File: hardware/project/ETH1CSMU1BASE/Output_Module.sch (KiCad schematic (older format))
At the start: 64 parts

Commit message: Power supply design
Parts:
- removed HS?: Heatsink, symbol Mechanical:Heatsink
- added HS901: Heatsink_Pad, symbol Mechanical:Heatsink_Pad
- C910, C911: renamed from C?; value 10n -> 10n/400V
- Q915, Q916: renamed from Q?; value Q_PMOS_GDS -> IRF9630SPBF
- R925, R926: renamed from R?; value 26R1/10W -> 26R1/5W
- gave numbers to parts that had none: 57
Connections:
- net labels added: GNDF, GNDO
- net labels removed: GNDHV
- wire segments 209 -> 211

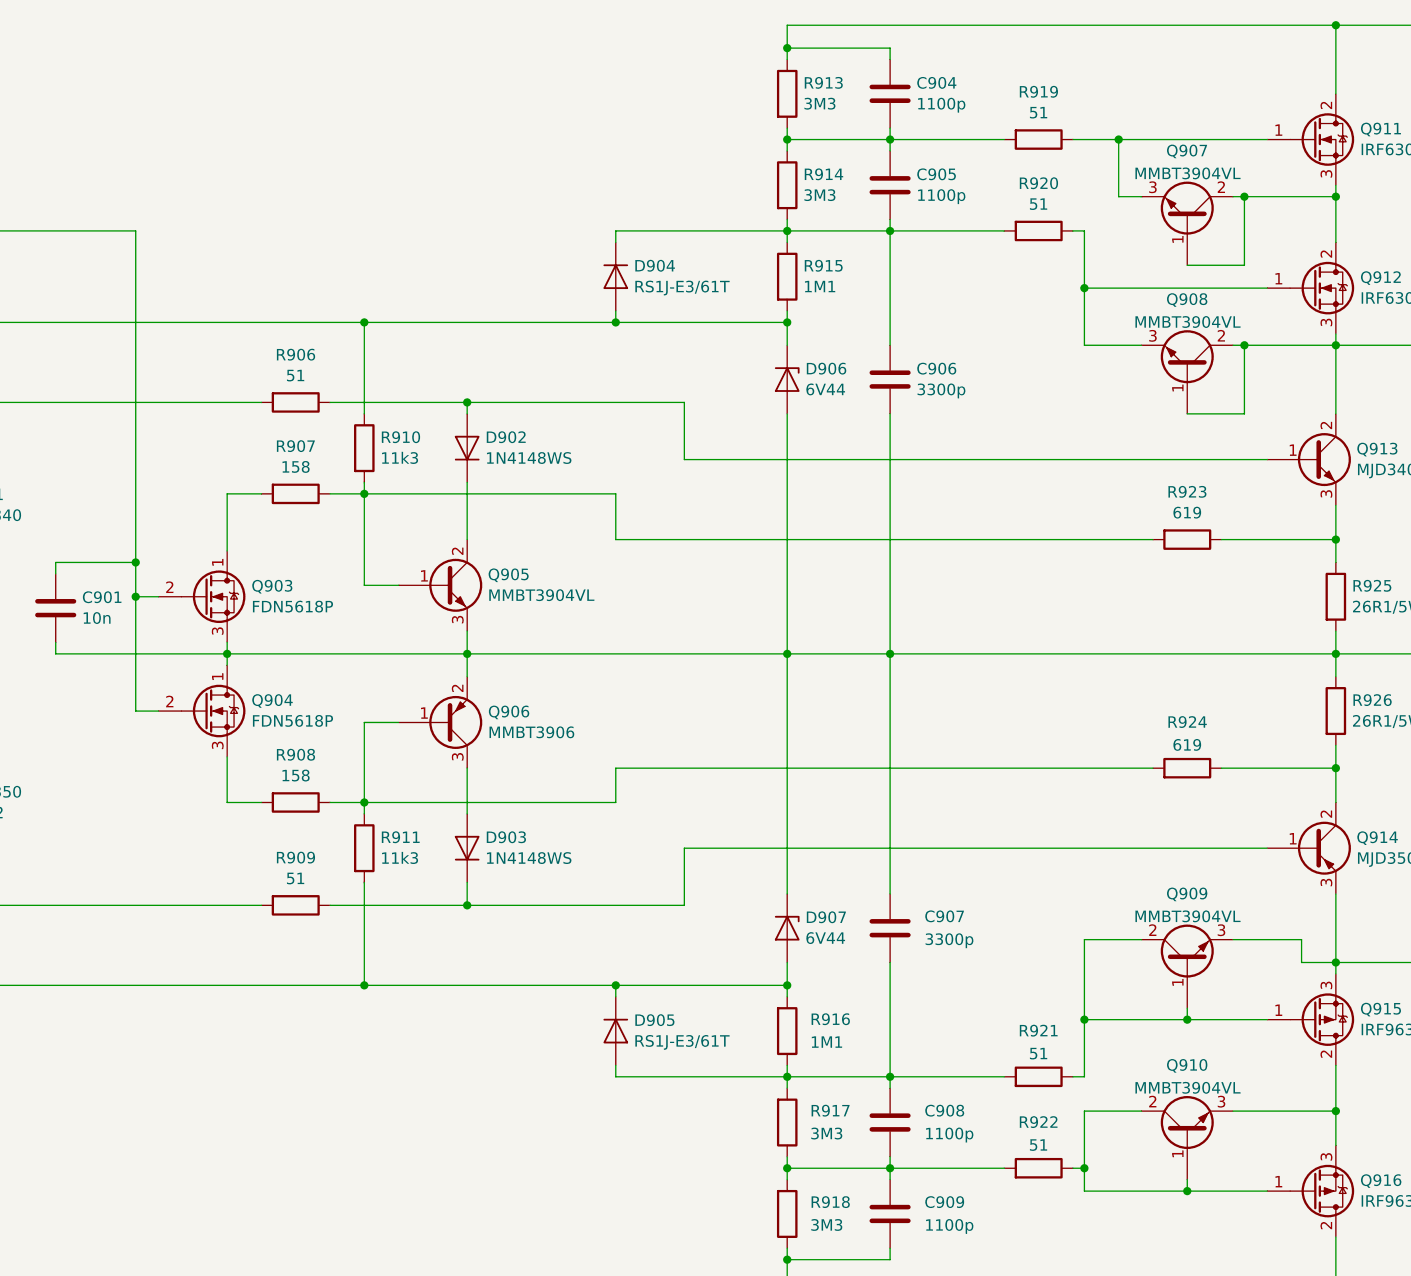
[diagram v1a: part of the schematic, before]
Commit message: Footprint assigment
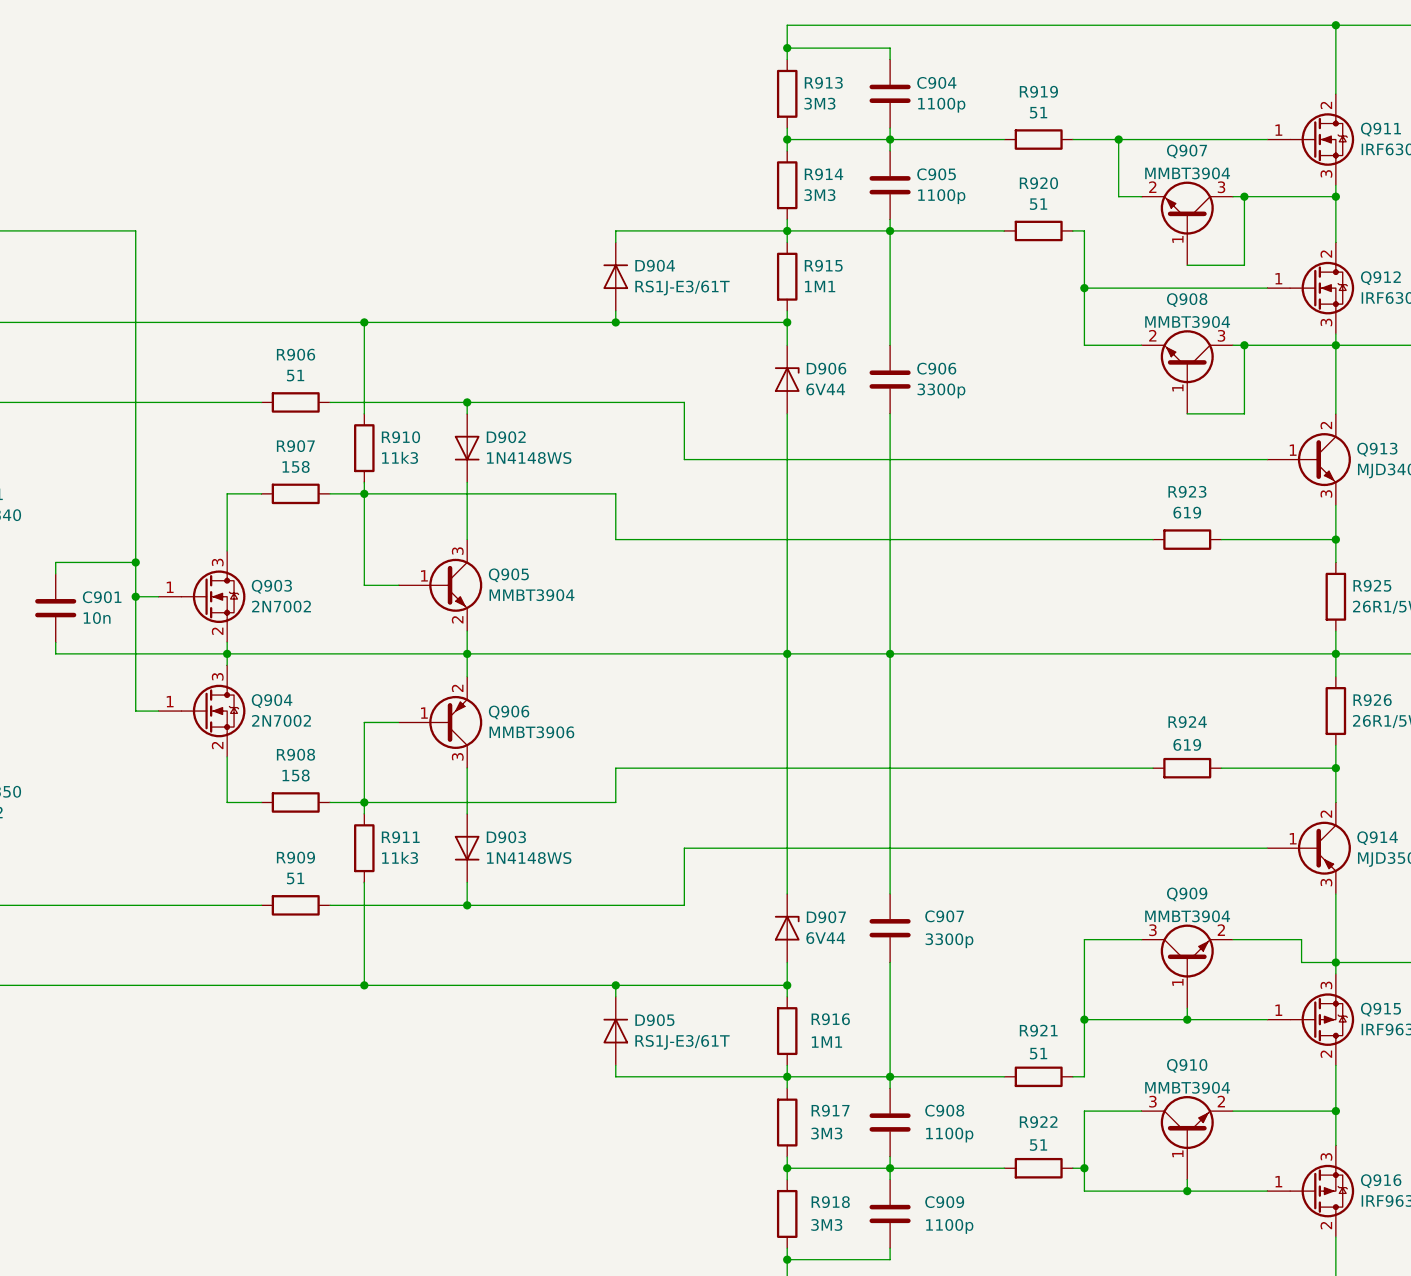
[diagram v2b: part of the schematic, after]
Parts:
- removed Q903, Q904: FDN5618P, symbol Device:Q_NMOS_DGS
- removed Q905, Q907, Q908, Q909, Q910: MMBT3904VL, symbol Device:Q_NPN_BCE
- added Q903, Q904: 2N7002, Package_TO_SOT_SMD:SOT-23, symbol Transistor_FET:2N7002
- added Q905, Q907, Q908, Q909, Q910: MMBT3904, Package_TO_SOT_SMD:SOT-23, symbol Transistor_BJT:MMBT3904
- C902, C903: footprint (none) -> Capacitor_SMD:C_0603_1608Metric_Pad1.05x0.95mm_HandSolder
- Q901, Q902, Q913, Q914: footprint (none) -> Package_TO_SOT_SMD:TO-252-2
- Q911, Q912, Q915, Q916: footprint (none) -> Package_TO_SOT_SMD:TO-263-2
- R901, R902: footprint (none) -> Resistor_SMD:R_0603_1608Metric_Pad1.05x0.95mm_HandSolder
- R903, R904, R905, R906, R907, R908, R909, R910, R911, R912, R913, R914, R915, R916, R917, R918, R919, R920, R921, R922, R923, R924: footprint (none) -> Resistor_SMD:R_0805_2012Metric_Pad1.15x1.40mm_HandSolder
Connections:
- net 100mA_BIAS: now also Q903.1 (G), Q904.1 (G)
- net GNDF: now also Q903.2 (S), Q904.3 (D), Q905.2 (E)
- net at Q911.1 (G), R919.1: now also Q907.2 (E)
- net at Q911.3 (S), Q912.2 (D): now also Q907.1 (B), Q907.3 (C)
- net at Q912.1 (G), R920.1: now also Q908.2 (E)
- net at D909.1 (K), Q912.3 (S), Q913.2 (C): now also Q908.1 (B), Q908.3 (C)
- net at R907.1, R910.2, R923.2: now also Q905.1 (B)
- net at D910.2 (A), Q914.3 (E), Q915.3 (S): now also Q909.2 (E)
- net at Q916.1 (G), R922.1: now also Q910.1 (B), Q910.3 (C)
- net at Q915.1 (G), R921.1: now also Q909.1 (B), Q909.3 (C)
- net at Q915.2 (D), Q916.3 (S): now also Q910.2 (E)
- net at R907.2: now also Q903.3 (D)
- net at R908.2: now also Q904.2 (S)
- net at D902.1 (K): now also Q905.3 (C)

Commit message: Footprint assignment
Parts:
- C701: renamed from C901; footprint (none) -> Capacitor_SMD:C_1206_3216Metric_Pad1.42x1.75mm_HandSolder
- C704: renamed from C904; footprint (none) -> Capacitor_SMD:C_1206_3216Metric_Pad1.42x1.75mm_HandSolder
- C705: renamed from C905; footprint (none) -> Capacitor_SMD:C_1206_3216Metric_Pad1.42x1.75mm_HandSolder
- C706: renamed from C906; footprint (none) -> Capacitor_SMD:C_0805_2012Metric_Pad1.15x1.40mm_HandSolder
- C707: renamed from C907; footprint (none) -> Capacitor_SMD:C_0805_2012Metric_Pad1.15x1.40mm_HandSolder
- C708: renamed from C908; footprint (none) -> Capacitor_SMD:C_1206_3216Metric_Pad1.42x1.75mm_HandSolder
- C709: renamed from C909; footprint (none) -> Capacitor_SMD:C_1206_3216Metric_Pad1.42x1.75mm_HandSolder
- C710: renamed from C910; footprint (none) -> Capacitor_SMD:C_0805_2012Metric_Pad1.15x1.40mm_HandSolder
- C711: renamed from C911; footprint (none) -> Capacitor_SMD:C_0805_2012Metric_Pad1.15x1.40mm_HandSolder
- D701: renamed from D901; value BZT52B15LP -> 1N718; footprint (none) -> Diode_SMD:D_MELF_Handsoldering
- D702: renamed from D902; footprint (none) -> Diode_SMD:D_SOD-123
- D703: renamed from D903; footprint (none) -> Diode_SMD:D_SOD-123
- D704: renamed from D904; footprint (none) -> Diode_SMD:D_SMA
- D705: renamed from D905; footprint (none) -> Diode_SMD:D_SMA
- D706: renamed from D906; footprint (none) -> ETH1CSMU1:DO-219AC
- D707: renamed from D907; footprint (none) -> ETH1CSMU1:DO-219AC
- D708: renamed from D908; value BZT52B15LP -> 1N718; footprint (none) -> Diode_SMD:D_MELF_Handsoldering
- D709: renamed from D909; footprint (none) -> ETH1CSMU1:D_SOD-128
- D710: renamed from D910; footprint (none) -> ETH1CSMU1:D_SOD-128
- R705: renamed from R905; value 3k57 -> 3k57/0.5W
- R712: renamed from R912; value 3k57 -> 3k57/0.5W
- R725: renamed from R925; value 26R1/5W -> 26R1/1W; footprint (none) -> Resistor_SMD:R_2010_5025Metric_Pad1.52x2.65mm_HandSolder
- R726: renamed from R926; value 26R1/5W -> 26R1/1W; footprint (none) -> Resistor_SMD:R_2010_5025Metric_Pad1.52x2.65mm_HandSolder
- renumbered C902 to C702, C903 to C703, HS901 to HS701, Q901 to Q701, Q902 to Q702, Q903 to Q703, Q904 to Q704, Q905 to Q705, Q906 to Q706, Q907 to Q707, Q908 to Q708, Q909 to Q709, Q910 to Q710, Q911 to Q711, Q912 to Q712, Q913 to Q713, Q914 to Q714, Q915 to Q715, Q916 to Q716, R901 to R701, R902 to R702, R903 to R703, R904 to R704, R906 to R706, R907 to R707, R908 to R708, R909 to R709, R910 to R710, R911 to R711, R913 to R713, R914 to R714, R915 to R715, R916 to R716, R917 to R717, R918 to R718, R919 to R719, R920 to R720, R921 to R721, R922 to R722, R923 to R723, R924 to R724
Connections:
- net -HV: now also Q716.2 (D)
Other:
- note added: "6V44 - PLZ6V2C-G3/H"
